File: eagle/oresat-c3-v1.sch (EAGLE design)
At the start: 173 parts, among them J1 J-SAMTEC-TFM-110-X1-XXX-D-RA, J12 U.FL, J13 U.FL, J14 U.FL, J15 HARWIN-2X8X1.27, J16 U.FL, J17 U.FL, J18 U.FL, J19 HARWIN-2X8X1.27, J2 U.FL, J3 U.FL, J4 U.FL, J6 J-SAMTEC-TFM-120-X1-XXX-D-RA, J7 FTSH-105-XX-X-DV-K, Q1 MOSFET-PCH-SOT23-6, U1 MAX892LEUA+T21-0036K-L, U11 U-ONSEMI-AX5043, U12 LP2985XX-N, U13 U-ONSEMI-AX5043, U14 LP2985XX-N, U2 TCAN330, U3 TCAN330, U4 TPS259621 - eFuse, U5 TPS62111RSA, U6 MAX6374KA-T21-0078H-L, U7 STM32F446RE, U9 SFEM016GB1EM1TO-A-HG-111-STD, X1 16MHZ-2.5x2mm, X3 TAITIEN-TY, X4 TAITIEN-TY

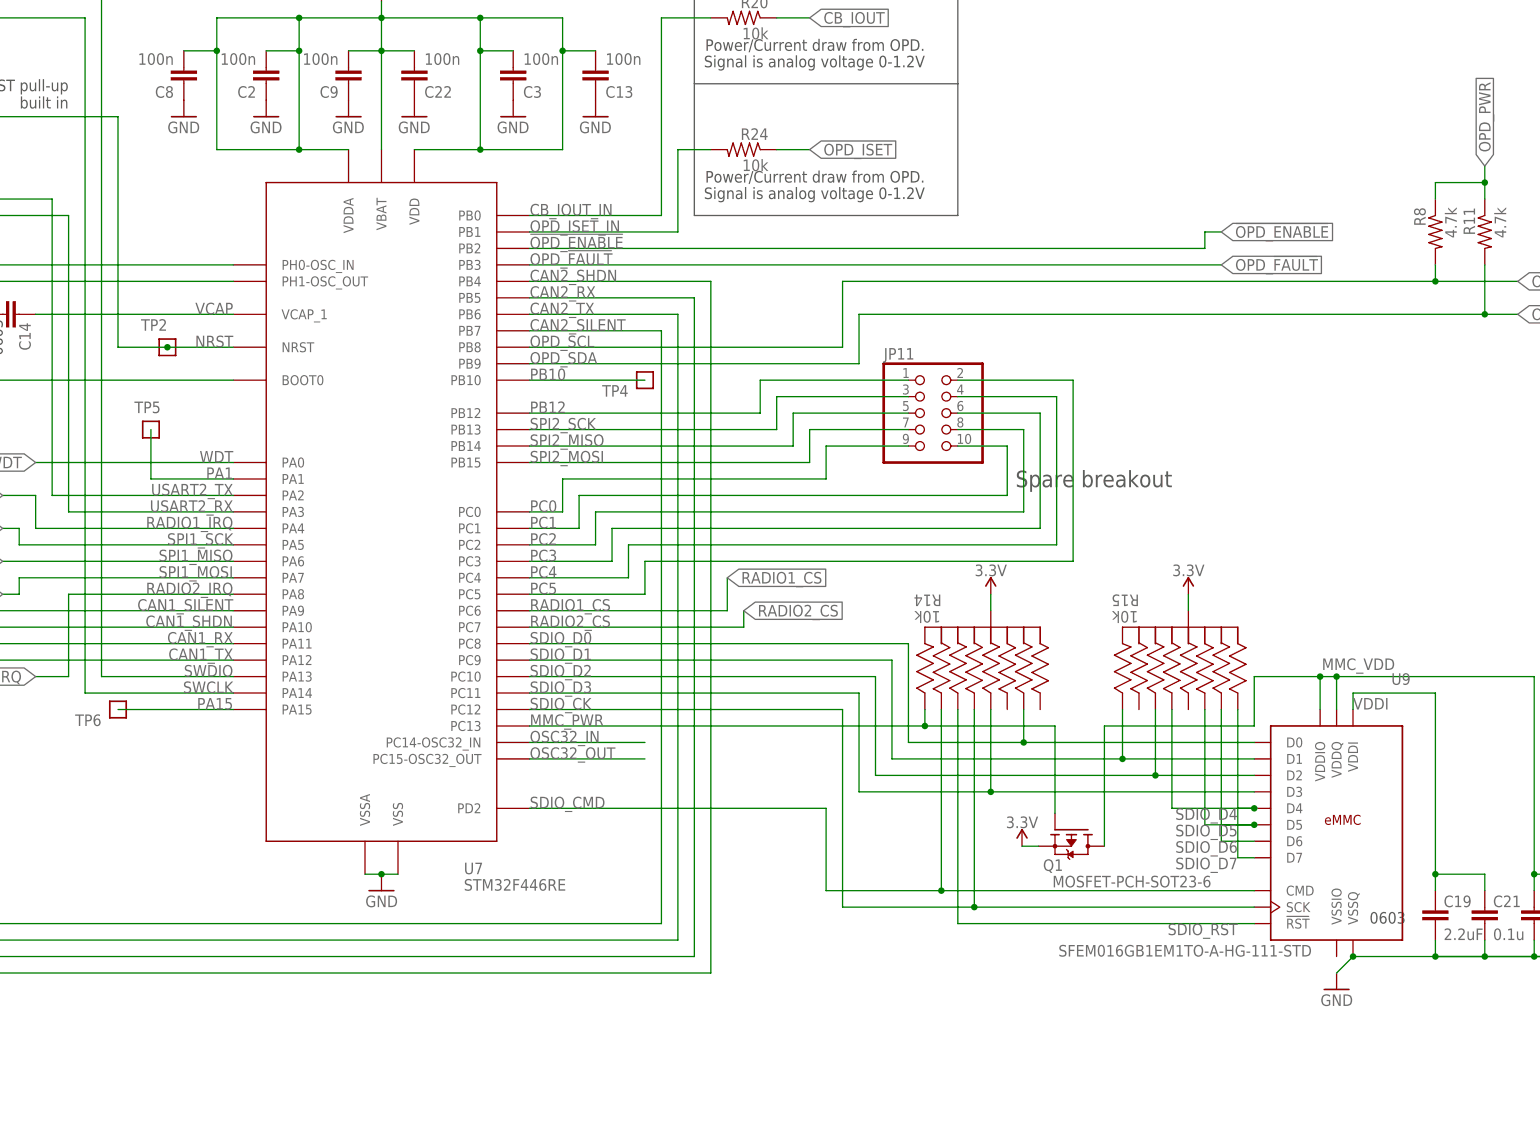
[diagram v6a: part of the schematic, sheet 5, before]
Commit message: Made Design review changes to C3 board
updated changes made in design review doc
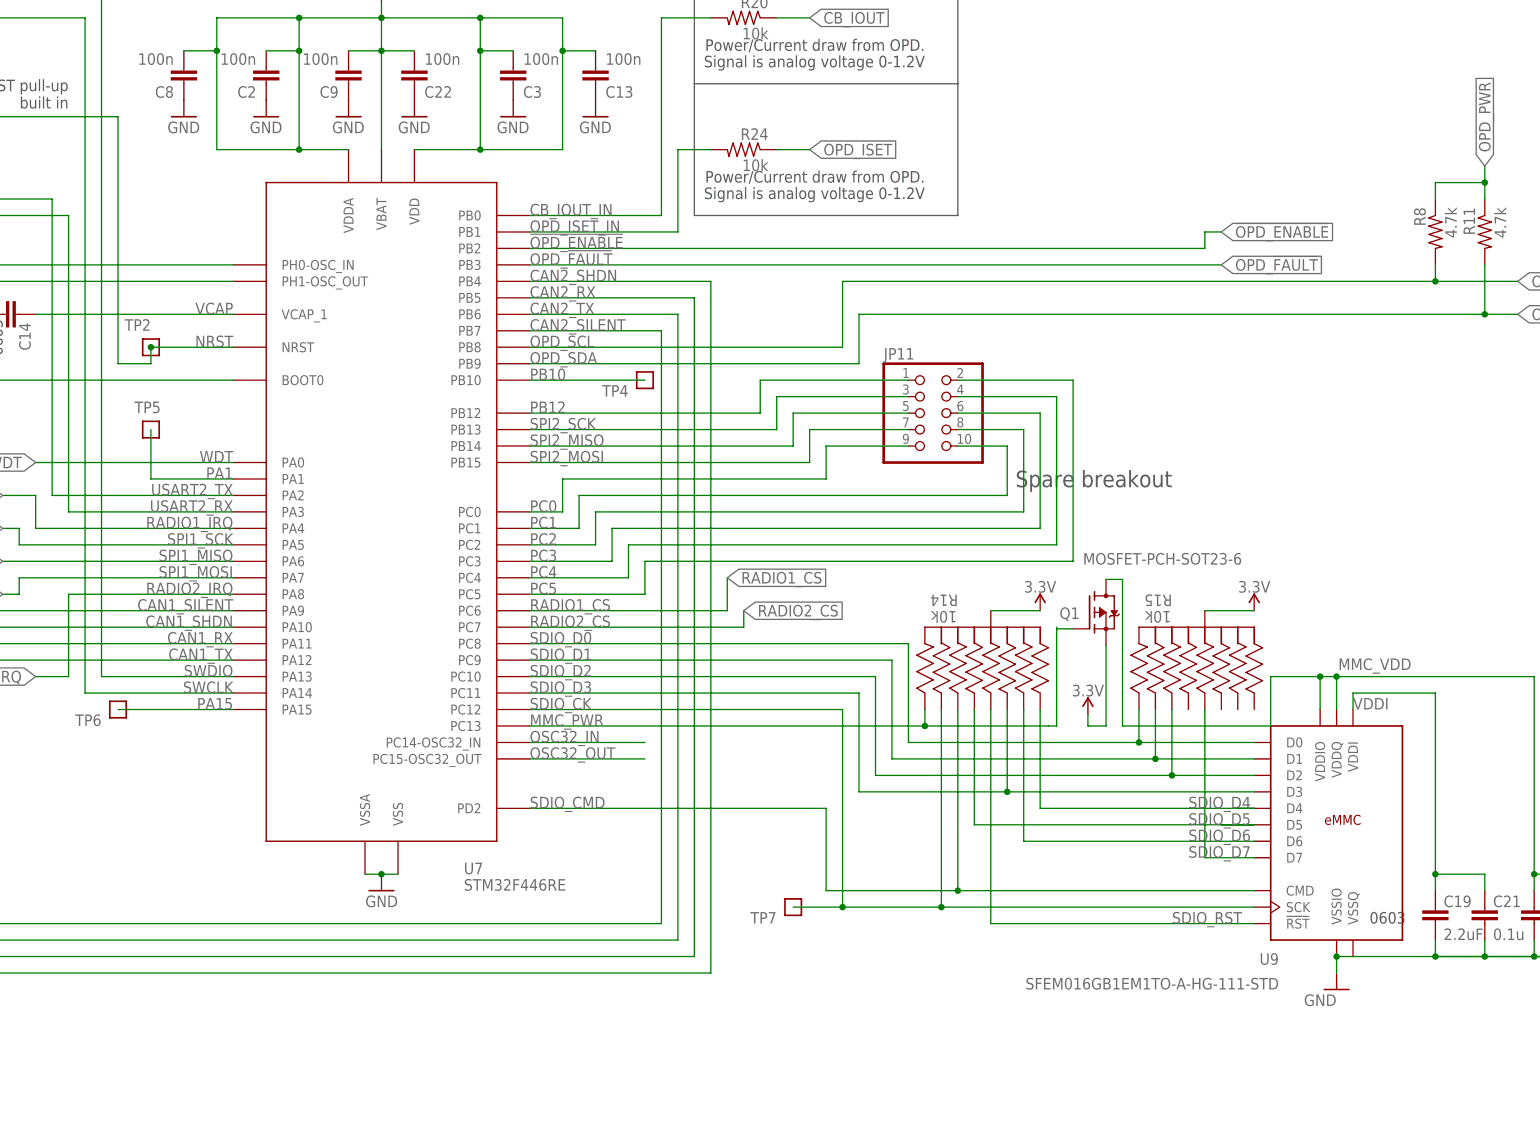
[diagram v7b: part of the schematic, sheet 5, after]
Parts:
- removed J12, J16, J17, J18: U.FL, SparkFun-Connectors:U.FL
- added J10, J11, J8, J9: U.FL, SparkFun-Connectors:U.FL2PIN
- added TP7: TEST-POINT, Tova:TEST-POINT
- J13, J14: device SparkFun-Connectors:U.FL -> SparkFun-Connectors:U.FL2PIN
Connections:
- removed net RX2: C64.1, J16.SIGNAL
- new net N$2: C64.1, J11.SIGNAL
- new net N$4: R14.66
- net GND: now also J10.GND, J11.GND, J13.GND, J14.GND, J15.13, J15.14, J15.16, J19.13, J19.14, J19.16, J8.GND, J9.GND
- net RX1: now also J10.SIGNAL; no longer J12.SIGNAL
- net SDIO_CK: now also R14.99, TP7.1; no longer R14.88
- net SDIO_CMD: now also R14.22; no longer R14.99
- net SDIO_D0: now also R15.11; no longer R14.44
- net SDIO_D1: now also R15.99; no longer R15.11
- net SDIO_D3: now also R14.77; no longer R14.33
- net SDIO_D4: no longer R15.88
- net SDIO_D5: now also R14.88; no longer R15.77
- net SDIO_D6: now also R14.44; no longer R15.44
- net SDIO_D7: now also R15.33; no longer R15.66
- net SDIO_RST: now also R14.33; no longer R14.22
- net SYSCLK1: now also J8.SIGNAL; no longer J14.SIGNAL
- net SYSCLK2: now also J14.SIGNAL; no longer J18.SIGNAL
- net TX1: now also J9.SIGNAL; no longer J13.SIGNAL
- net TX2: now also J13.SIGNAL; no longer J17.SIGNAL
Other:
- moved on the sheet: Q1, R15, TP2

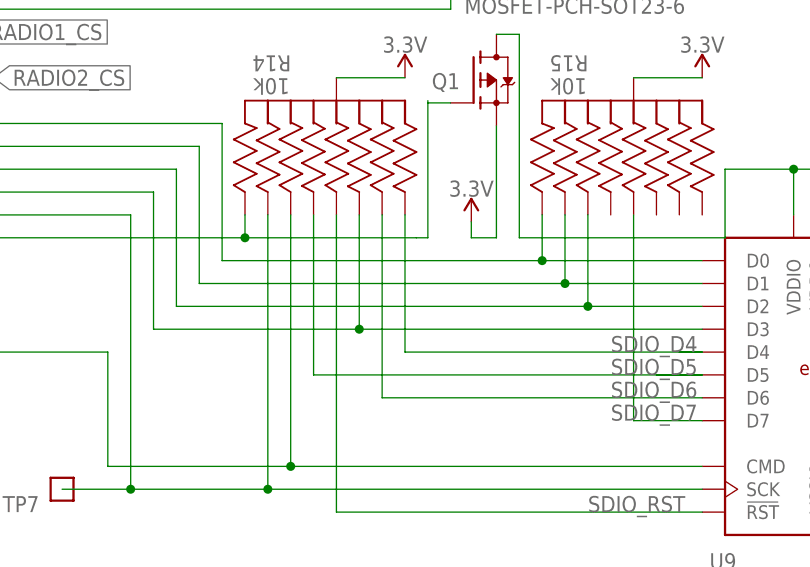
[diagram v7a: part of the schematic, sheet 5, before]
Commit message: Fix net error
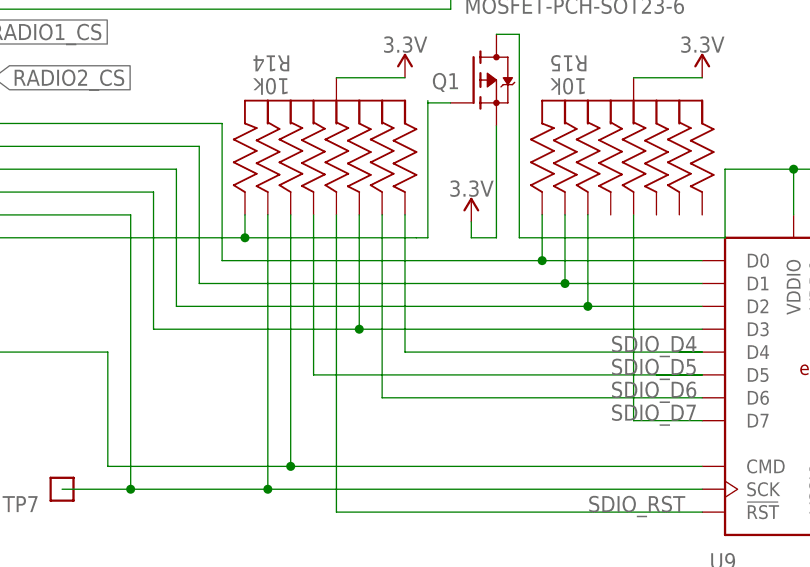
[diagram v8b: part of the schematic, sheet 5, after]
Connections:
- removed net N$4: R14.66
- net SDIO_D4: now also R14.66
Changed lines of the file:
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@@
 <pinref part="U9" gate="U" pin="D4"/>
 <wire x1="314.96" y1="68.58" x2="347.98" y2="68.58" width="0.1524" layer="91"/>
-<wire x1="314.96" y1="81.1276" x2="314.96" y2="68.58" width="0.1524" layer="91"/>
+<pinref part="R14" gate="A" pin="66"/>
+<wire x1="314.96" y1="68.58" x2="314.96" y2="83.82" width="0.1524" layer="91"/>
 </segment>
 </net>
@@
 </segment>
 </net>
-<net name="N$4" class="0">
-<segment>
-<pinref part="R14" gate="A" pin="66"/>
-<wire x1="314.96" y1="83.82" x2="314.96" y2="81.4324" width="0.1524" layer="91"/>
-</segment>
-</net>
